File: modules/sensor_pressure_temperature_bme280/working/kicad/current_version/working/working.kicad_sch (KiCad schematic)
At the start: 6 parts, among them U1 isn280

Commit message: fixed formatting to be more consistent
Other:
- note added: "extra"
- note added: "sensor_pressure_temperature_bme280"
- note removed: "name"
- moved on the sheet: C1, C2, R1, R2, R3, U1

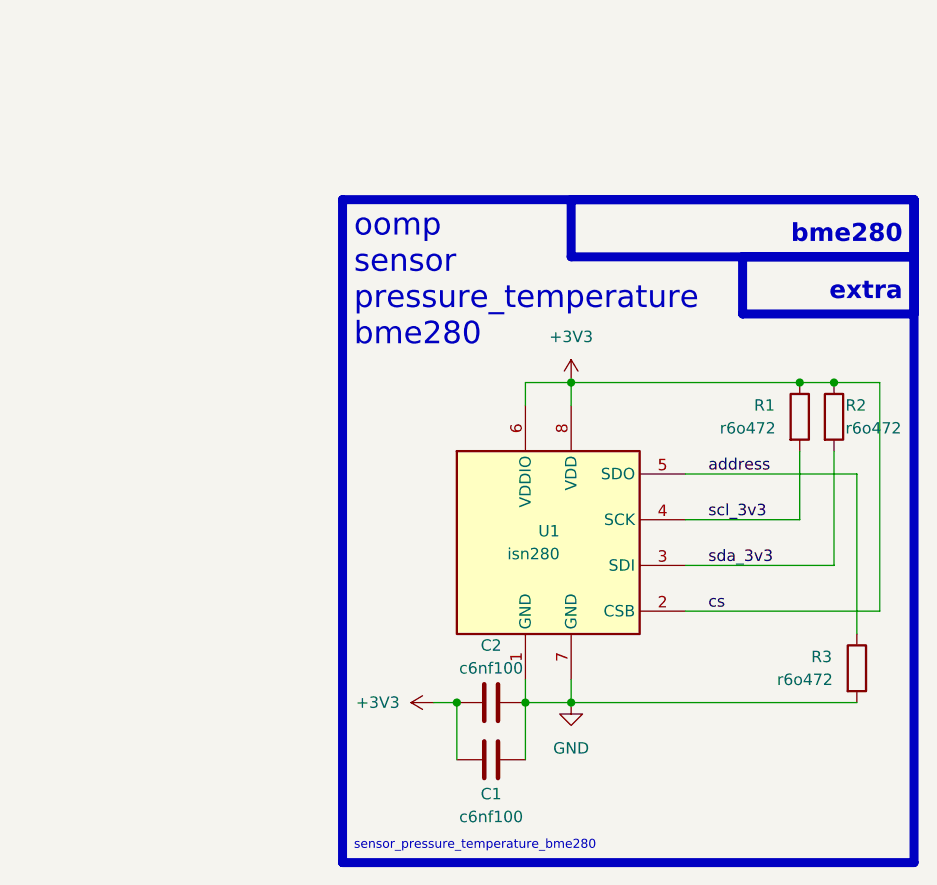
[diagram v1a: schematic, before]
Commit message: schematic formatting
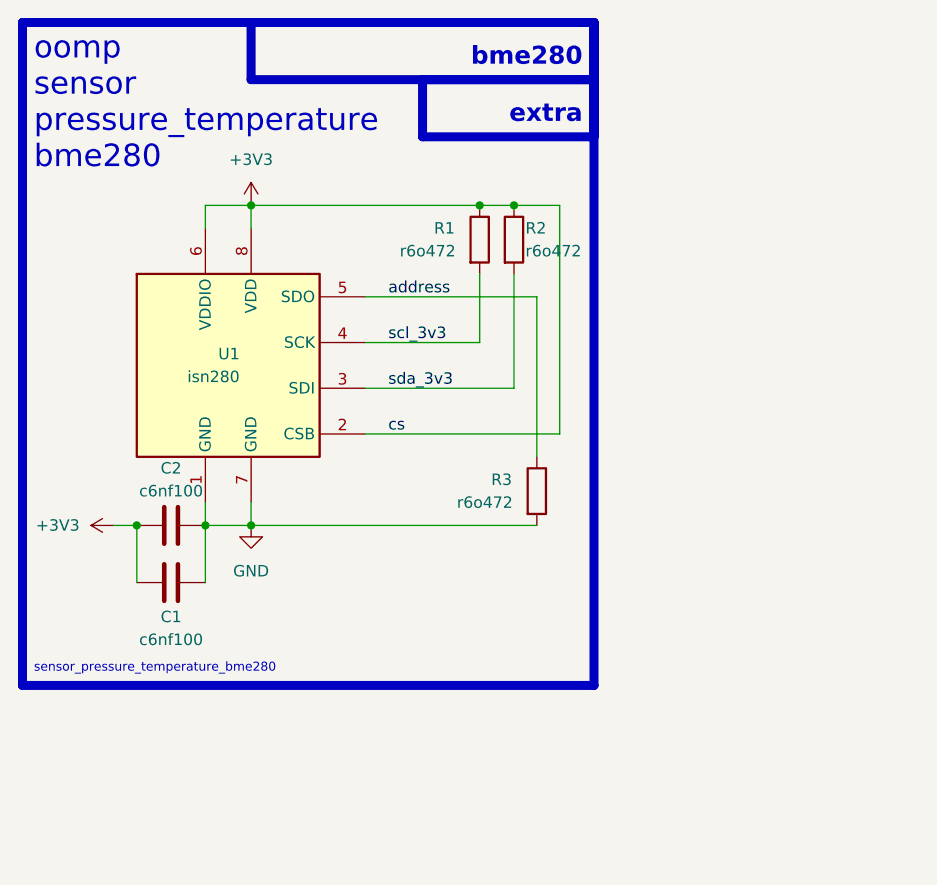
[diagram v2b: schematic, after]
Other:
- moved on the sheet: C1, C2, R1, R2, R3, U1
